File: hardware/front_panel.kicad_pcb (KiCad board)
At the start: 2 copper layers, 9.8 x 128.5 mm, 4 parts

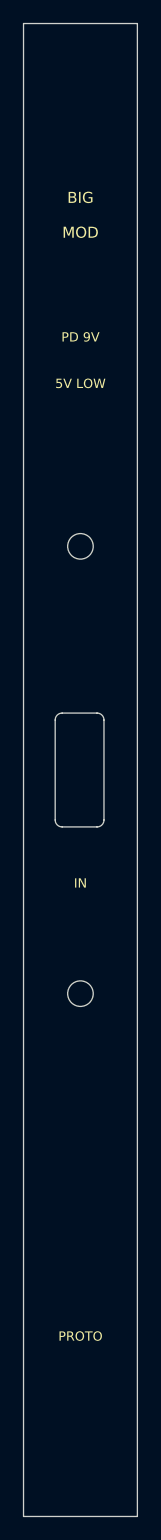
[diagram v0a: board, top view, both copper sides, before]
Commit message: WIP: consolidate PD-only Eurorack circuit on one sheet and dimension 2HP assembly
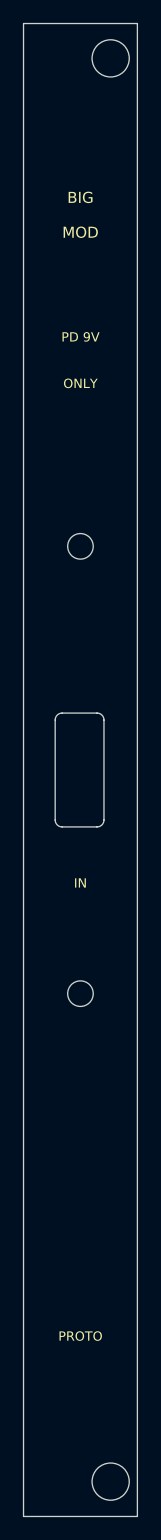
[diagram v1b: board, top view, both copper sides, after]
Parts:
- moved H1 2.60 mm to (57.5, 33.0)
- moved H2 2.60 mm to (57.5, 155.5)
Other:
- board text added: "Doepfer X=7.5 / dia3.2: 0.7mm FR4 web; M3 head overhang BLOCKER"
- board text added: "Mounting proposal: ../docs/assembly.svg / mechanics.md"
- board text added: "ONLY"
- board text removed: "5V LOW"
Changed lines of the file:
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@@
 	(footprint ""
 		(layer "F.Cu")
-		(at 54.9 113.5)
-		(property "Reference" "H4"
+		(at 57.5 155.5)
+		(property "Reference" "H2"
+			(at 0 0 0)
+			(layer "F.SilkS")
+			(hide yes)
+			(effects
+				(font
+					(size 1.27 1.27)
+				)
+			)
+		)
+		(property "Value" "MECHANICAL_NPTH"
+			(at 0 0 0)
+			(layer "F.Fab")
+			(hide yes)
+			(effects
+				(font
+					(size 1.27 1.27)
+				)
+			)
+		)
+		(property "Datasheet" ""
+			(at 0 0 0)
+			(layer "F.Fab")
+			(hide yes)
+			(effects
+				(font
+					(size 1.27 1.27)
+				)
+			)
+		)
+		(property "Description" ""
+			(at 0 0 0)
+			(layer "F.Fab")
+			(hide yes)
+			(effects
+				(font
+					(size 1.27 1.27)
+				)
+			)
+		)
+		(duplicate_pad_numbers_are_jumpers no)
+		(pad "" np_thru_hole circle
+			(at 0 0)
+			(size 3.2 3.2)
+			(drill 3.2)
+			(layers "*.Cu")
+		)
+		(embedded_fonts no)
+	)
+	(footprint ""
+		(layer "F.Cu")
+		(at 57.5 33)
+		(property "Reference" "H1"
+			(at 0 0 0)
+			(layer "F.SilkS")
+			(hide yes)
+			(effects
+				(font
+					(size 1.27 1.27)
+				)
+			)
+		)
+		(property "Value" "MECHANICAL_NPTH"
+			(at 0 0 0)
+			(layer "F.Fab")
+			(hide yes)
+			(effects
+				(font
+					(size 1.27 1.27)
+				)
+			)
+		)
+		(property "Datasheet" ""
+			(at 0 0 0)
+			(layer "F.Fab")
+			(hide yes)
+			(effects
+				(font
+					(size 1.27 1.27)
+				)
+			)
+		)
+		(property "Description" ""
+			(at 0 0 0)
+			(layer "F.Fab")
+			(hide yes)
+			(effects
+				(font
+					(size 1.27 1.27)
+				)
+			)
+		)
+		(duplicate_pad_numbers_are_jumpers no)
+		(pad "" np_thru_hole circle
+			(at 0 0)
+			(size 3.2 3.2)
+			(drill 3.2)
+			(layers "*.Cu")
+		)
+		(embedded_fonts no)
+	)
+	(footprint ""
+		(layer "F.Cu")
+		(at 54.9 75)
+		(property "Reference" "H3"
 			(at 0 0 0)
 			(layer "F.SilkS")
@@
 	(footprint ""
 		(layer "F.Cu")
-		(at 54.9 75)
-		(property "Reference" "H3"
+		(at 54.9 113.5)
+		(property "Reference" "H4"
 			(at 0 0 0)
 			(layer "F.SilkS")
@@
 		(embedded_fonts no)
 	)
-	(footprint ""
-		(layer "F.Cu")
-		(at 54.9 33)
-		(property "Reference" "H1"
-			(at 0 0 0)
-			(layer "F.SilkS")
-			(hide yes)
-			(effects
-				(font
-					(size 1.27 1.27)
-				)
-			)
-		)
-		(property "Value" "MECHANICAL_NPTH"
-			(at 0 0 0)
-			(layer "F.Fab")
-			(hide yes)
-			(effects
-				(font
-					(size 1.27 1.27)
-				)
-			)
-		)
-		(property "Datasheet" ""
-			(at 0 0 0)
-			(layer "F.Fab")
-			(hide yes)
-			(effects
-				(font
-					(size 1.27 1.27)
-				)
-			)
-		)
-		(property "Description" ""
-			(at 0 0 0)
-			(layer "F.Fab")
-			(hide yes)
-			(effects
-				(font
-					(size 1.27 1.27)
-				)
-			)
-		)
-		(duplicate_pad_numbers_are_jumpers no)
-		(pad "" np_thru_hole oval
-			(at 0 0)
-			(size 5 3.2)
-			(drill oval 5 3.2)
-			(layers "*.Cu")
-			(thermal_bridge_angle 45)
-		)
-		(embedded_fonts no)
-	)
-	(footprint ""
-		(layer "F.Cu")
-		(at 54.9 155.5)
-		(property "Reference" "H2"
-			(at 0 0 0)
-			(layer "F.SilkS")
-			(hide yes)
-			(effects
-				(font
-					(size 1.27 1.27)
-				)
-			)
-		)
-		(property "Value" "MECHANICAL_NPTH"
-			(at 0 0 0)
-			(layer "F.Fab")
-			(hide yes)
-			(effects
-				(font
-					(size 1.27 1.27)
-				)
-			)
-		)
-		(property "Datasheet" ""
-			(at 0 0 0)
-			(layer "F.Fab")
-			(hide yes)
-			(effects
-				(font
-					(size 1.27 1.27)
-				)
-			)
-		)
-		(property "Description" ""
-			(at 0 0 0)
-			(layer "F.Fab")
-			(hide yes)
-			(effects
-				(font
-					(size 1.27 1.27)
-				)
-			)
-		)
-		(duplicate_pad_numbers_are_jumpers no)
-		(pad "" np_thru_hole oval
-			(at 0 0)
-			(size 5 3.2)
-			(drill oval 5 3.2)
-			(layers "*.Cu")
-			(thermal_bridge_angle 45)
-		)
-		(embedded_fonts no)
-	)
 	(gr_line
 		(start 50 30)
@@
 		)
 	)
-	(gr_text "5V LOW"
+	(gr_text "ONLY"
 		(at 54.9 61 0)
 		(layer "F.SilkS")
@@
 				(thickness 0.12)
 			)
+		)
+	)
+	(gr_text "Mounting proposal: ../docs/assembly.svg / mechanics.md"
+		(at 112 70 0)
+		(layer "Dwgs.User")
+		(effects
+			(font
+				(size 0.85 0.85)
+				(thickness 0.12)
+			)
+		)
+	)
+	(gr_text "Doepfer X=7.5 / dia3.2: 0.7mm FR4 web; M3 head overhang BLOCKER"
+		(at 114 65 0)
+		(layer "Dwgs.User")
+		(effects
+			(font
+				(size 0.85 0.85)
+				(thickness 0.12)
+			)

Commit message: Update on the PCB.
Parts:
- added H5: MECHANICAL_NPTH, , F.Cu at (56.7, 68.0)
- added H6: MECHANICAL_NPTH, , F.Cu at (56.4, 121.0)
- moved H3 23.0 mm to (56.4, 52.0)
- moved H4 23.0 mm to (56.4, 136.5)
- moved H1 5.08 mm to (52.4, 33.0)
- moved H2 5.08 mm to (52.4, 155.5)
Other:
- outline, holes or cut-outs redrawn
- board text added: "2HP / round corner holes X2.42 = X7.50 minus one 5.08mm rail pitch"
- board text added: "A4.2"
- board text added: "A4.2 plain L brackets: M3x8 panel / M3x8 countersunk side"
- board text added: "PWR"
- board text added: "RESET"
- board text added: "TL3340AF160QG SMT recessed reset; 3mm THT LED formed 90 degrees"
- board text added: "USB"
- board text removed: "2HP: 9.8 x 128.5 x 1.6 mm"
- board text removed: "Doepfer X=7.5 / dia3.2: 0.7mm FR4 web; M3 head overhang BLOCKER"
- board text removed: "Front face Z=0; inward +Z; NO copper"
- board text removed: "IN"
- board text removed: "Mounting proposal: ../docs/assembly.svg / mechanics.md"
- board text removed: "ONLY"
- board text removed: "PROTO"
- board text removed: "Port axis (X,Y,Z)=(4.900,64.250,0.800)"
- board text removed: "USB cutout: 4.2 x 9.8, R0.6"

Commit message: Save 9 V power-supply schematic prototype and LED mechanical provisions
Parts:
- added H7: MECHANICAL_NPTH, , F.Cu at (56.7, 76.0)
- added H8: MECHANICAL_NPTH, , F.Cu at (56.7, 84.0)
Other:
- board text added: "+12V"
- board text added: "+5V"
- board text added: "-12V"
- board text added: "TL3340AF160QG SMT reset; D10/D11/D12 RED 3mm LEDs formed 90 degrees"
- board text removed: "PWR"
- board text removed: "TL3340AF160QG SMT recessed reset; 3mm THT LED formed 90 degrees"
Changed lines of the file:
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@@
+	(footprint ""
+		(layer "F.Cu")
+		(at 56.7 84)
+		(property "Reference" "H8"
+			(at 0 0 0)
+			(layer "F.SilkS")
+			(hide yes)
+			(effects
+				(font
+					(size 1.27 1.27)
+				)
+			)
+		)
+		(property "Value" "MECHANICAL_NPTH"
+			(at 0 0 0)
+			(layer "F.Fab")
+			(hide yes)
+			(effects
+				(font
+					(size 1.27 1.27)
+				)
+			)
+		)
+		(property "Datasheet" ""
+			(at 0 0 0)
+			(layer "F.Fab")
+			(hide yes)
+			(effects
+				(font
+					(size 1.27 1.27)
+				)
+			)
+		)
+		(property "Description" ""
+			(at 0 0 0)
+			(layer "F.Fab")
+			(hide yes)
+			(effects
+				(font
+					(size 1.27 1.27)
+				)
+			)
+		)
+		(duplicate_pad_numbers_are_jumpers no)
+		(pad "" np_thru_hole circle
+			(at 0 0)
+			(size 3.6 3.6)
+			(drill 3.6)
+			(layers "*.Cu")
+		)
+		(embedded_fonts no)
+	)
 	(footprint ""
 		(layer "F.Cu")
@@
 		(at 56.7 68)
 		(property "Reference" "H5"
+			(at 0 0 0)
+			(layer "F.SilkS")
+			(hide yes)
+			(effects
+				(font
+					(size 1.27 1.27)
+				)
+			)
+		)
+		(property "Value" "MECHANICAL_NPTH"
+			(at 0 0 0)
+			(layer "F.Fab")
+			(hide yes)
+			(effects
+				(font
+					(size 1.27 1.27)
+				)
+			)
+		)
+		(property "Datasheet" ""
+			(at 0 0 0)
+			(layer "F.Fab")
+			(hide yes)
+			(effects
+				(font
+					(size 1.27 1.27)
+				)
+			)
+		)
+		(property "Description" ""
+			(at 0 0 0)
+			(layer "F.Fab")
+			(hide yes)
+			(effects
+				(font
+					(size 1.27 1.27)
+				)
+			)
+		)
+		(duplicate_pad_numbers_are_jumpers no)
+		(pad "" np_thru_hole circle
+			(at 0 0)
+			(size 3.6 3.6)
+			(drill 3.6)
+			(layers "*.Cu")
+		)
+		(embedded_fonts no)
+	)
+	(footprint ""
+		(layer "F.Cu")
+		(at 56.7 76)
+		(property "Reference" "H7"
 			(at 0 0 0)
 			(layer "F.SilkS")
@@
 		(layer "Edge.Cuts")
 	)
-	(gr_text "PWR"
-		(at 54.9 63 0)
+	(gr_text "+12V"
+		(at 54.9 64 0)
 		(layer "F.SilkS")
 		(effects
@@
 		)
 	)
-	(gr_text "PD 9V"
-		(at 54.9 84 0)
+	(gr_text "-12V"
+		(at 54.9 72 0)
+		(layer "F.SilkS")
+		(effects
+			(font
+				(size 0.8 0.8)
+				(thickness 0.12)
+			)
+		)
+	)
+	(gr_text "+5V"
+		(at 54.9 80 0)
 		(layer "F.SilkS")
 		(effects
@@
 		)
 	)
+	(gr_text "PD 9V"
+		(at 54.9 106.5 0)
+		(layer "F.SilkS")
+		(effects
+			(font
+				(size 0.8 0.8)
+				(thickness 0.12)
+			)
+		)
+	)
 	(gr_text "RESET"
 		(at 54.9 116 0)
@@
 		)
 	)
-	(gr_text "TL3340AF160QG SMT recessed reset; 3mm THT LED formed 90 degrees"
+	(gr_text "TL3340AF160QG SMT reset; D10/D11/D12 RED 3mm LEDs formed 90 degrees"
 		(at 100 48 0)
 		(layer "Dwgs.User")

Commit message: Replace MCU diagnostics with optional rail-sense IDC and single 5 V power LED
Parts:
- removed H7, H8: MECHANICAL_NPTH, 
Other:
- board text added: "+5V POWER"
- board text added: "TL3340AF160QG SMT reset; D10 RED 3mm +5V power LED formed 90 degrees"
- board text removed: "+12V"
- board text removed: "+5V"
- board text removed: "-12V"
- board text removed: "TL3340AF160QG SMT reset; D10/D11/D12 RED 3mm LEDs formed 90 degrees"

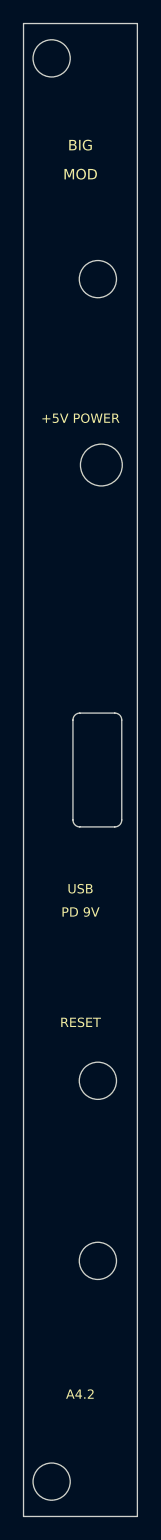
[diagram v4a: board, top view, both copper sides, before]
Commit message: Move USB, retry button and power LED to top; synchronize 64 V1 footprints without routing
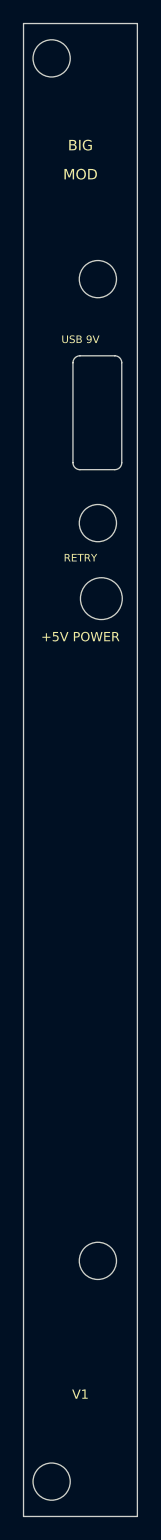
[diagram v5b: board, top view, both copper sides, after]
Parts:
- moved ? 48.0 mm to (56.4, 73.0)
- moved ? 11.5 mm to (56.7, 79.5)
- renumbered H3 to ?, H4 to ?, H1 to ?, H6 to ?, H2 to ?, H5 to ?
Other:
- outline, holes or cut-outs redrawn
- board text added: "RETRY"
- board text added: "USB 9V"
- board text added: "V1"
- board text removed: "A4.2"
- board text removed: "PD 9V"
- board text removed: "RESET"
- board text removed: "USB"

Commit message: Swap retry switch and power LED positions on carrier and front panel
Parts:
- moved ? 6.50 mm to (56.4, 79.5)
- moved ? 6.50 mm to (56.7, 73.0)
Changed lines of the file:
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@@
 	(footprint ""
 		(layer "F.Cu")
-		(at 56.4 73)
+		(at 56.4 79.5)
 		(property "Reference" ""
 			(at 0 0 0)
@@
 	(footprint ""
 		(layer "F.Cu")
-		(at 56.7 79.5)
+		(at 56.7 73)
 		(property "Reference" ""
 			(at 0 0 0)
@@
 	)
 	(gr_text "RETRY"
-		(at 54.9 76 0)
+		(at 54.9 82.5 0)
 		(layer "F.SilkS")
 		(effects
@@
 	)
 	(gr_text "+5V POWER"
-		(at 54.9 82.8 0)
+		(at 54.9 76.3 0)
 		(layer "F.SilkS")
 		(effects

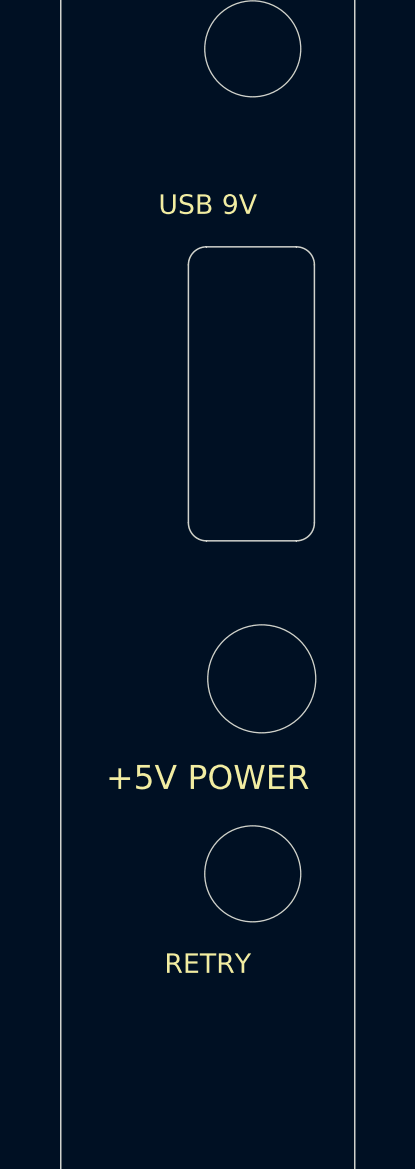
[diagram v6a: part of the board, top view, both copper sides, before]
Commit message: Complete four-layer routing, adopt proven HRO USB-C and release checked fabrication files
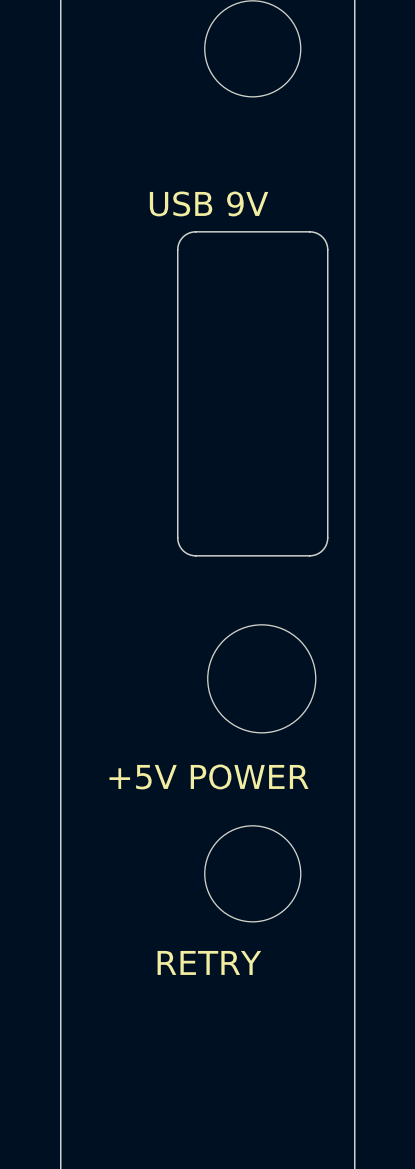
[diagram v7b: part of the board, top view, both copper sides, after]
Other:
- outline, holes or cut-outs redrawn
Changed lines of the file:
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@@
 	)
 	(setup
+		(stackup
+ (layer "F.SilkS" (type "Top Silk Screen") (color "White"))
+ (layer "F.Paste" (type "Top Solder Paste"))
+ (layer "F.Mask" (type "Top Solder Mask") (color "Black") (thickness 0.01))
+ (layer "F.Cu" (type "copper") (thickness 0))
+ (layer "dielectric 1" (type "core") (thickness 1.58) (material "FR4 Tg170") (epsilon_r 4.5) (loss_tangent 0.02))
+ (layer "B.Cu" (type "copper") (thickness 0))
+ (layer "B.Mask" (type "Bottom Solder Mask") (color "Black") (thickness 0.01))
+ (layer "B.Paste" (type "Bottom Solder Paste"))
+ (layer "B.SilkS" (type "Bottom Silk Screen") (color "White"))
+ (copper_finish "None") (dielectric_constraints no))
 		(pad_to_mask_clearance 0)
 		(allow_soldermask_bridges_in_footprints no)
@@
 		(attr board_only exclude_from_pos_files exclude_from_bom)
 		(duplicate_pad_numbers_are_jumpers no)
+		(fp_circle
+			(center 0 0)
+			(end 3.75 0)
+			(stroke
+				(width 0.05)
+				(type default)
+			)
+			(fill no)
+			(layer "F.CrtYd")
+		)
 		(pad "" np_thru_hole circle
 			(at 0 0)
@@
 		(attr board_only exclude_from_pos_files exclude_from_bom)
 		(duplicate_pad_numbers_are_jumpers no)
+		(fp_circle
+			(center 0 0)
+			(end 3.75 0)
+			(stroke
+				(width 0.05)
+				(type default)
+			)
+			(fill no)
+			(layer "F.CrtYd")
+		)
 		(pad "" np_thru_hole circle
 			(at 0 0)
@@
 		(attr board_only exclude_from_pos_files exclude_from_bom)
 		(duplicate_pad_numbers_are_jumpers no)
+		(fp_circle
+			(center 0 0)
+			(end 3.25 0)
+			(stroke
+				(width 0.05)
+				(type default)
+			)
+			(fill no)
+			(layer "F.CrtYd")
+		)
 		(pad "" np_thru_hole circle
 			(at 0 0)
@@
 		(attr board_only exclude_from_pos_files exclude_from_bom)
 		(duplicate_pad_numbers_are_jumpers no)
+		(fp_circle
+			(center 0 0)
+			(end 1.85 0)
+			(stroke
+				(width 0.05)
+				(type default)
+			)
+			(fill no)
+			(layer "F.CrtYd")
+		)
 		(pad "" np_thru_hole circle
 			(at 0 0)
@@
 		(attr board_only exclude_from_pos_files exclude_from_bom)
 		(duplicate_pad_numbers_are_jumpers no)
+		(fp_circle
+			(center 0 0)
+			(end 3.25 0)
+			(stroke
+				(width 0.05)
+				(type default)
+			)
+			(fill no)
+			(layer "F.CrtYd")
+		)
 		(pad "" np_thru_hole circle
 			(at 0 0)
@@
 		(attr board_only exclude_from_pos_files exclude_from_bom)
 		(duplicate_pad_numbers_are_jumpers no)
+		(fp_circle
+			(center 0 0)
+			(end 2.05 0)
+			(stroke
+				(width 0.05)
+				(type default)
+			)
+			(fill no)
+			(layer "F.CrtYd")
+		)
 		(pad "" np_thru_hole circle
 			(at 0 0)
@@
 	)
 	(gr_arc
-		(start 54.255 59.2)
-		(mid 54.430735 58.775735)
-		(end 54.855 58.6)
+		(start 53.9 58.7)
+		(mid 54.075735 58.275735)
+		(end 54.5 58.1)
 		(stroke
 			(width 0.05)
@@
 	)
 	(gr_line
-		(start 54.255 67.8)
-		(end 54.255 59.2)
+		(start 53.9 68.3)
+		(end 53.9 58.7)
 		(stroke
 			(width 0.05)
@@
 	)
 	(gr_line
-		(start 54.855 58.6)
-		(end 57.855 58.6)
+		(start 54.5 58.1)
+		(end 58.3 58.1)
 		(stroke
 			(width 0.05)
@@
 	)
 	(gr_arc
-		(start 54.855 68.4)
-		(mid 54.430735 68.224264)
-		(end 54.255 67.8)
+		(start 54.5 68.9)
+		(mid 54.075735 68.724264)
+		(end 53.9 68.3)
 		(stroke
 			(width 0.05)
@@
 	)
 	(gr_arc
-		(start 57.855 58.6)
-		(mid 58.279264 58.775735)
-		(end 58.455 59.2)
+		(start 58.3 58.1)
+		(mid 58.724264 58.275735)
+		(end 58.9 58.7)
 		(stroke
 			(width 0.05)
@@
 	)
 	(gr_line
-		(start 57.855 68.4)
-		(end 54.855 68.4)
+		(start 58.3 68.9)
+		(end 54.5 68.9)
 		(stroke
 			(width 0.05)
@@
 	)
 	(gr_line
-		(start 58.455 59.2)
-		(end 58.455 67.8)
+		(start 58.9 58.7)
+		(end 58.9 68.3)
 		(stroke
 			(width 0.05)
@@
 	)
 	(gr_arc
-		(start 58.455 67.8)
-		(mid 58.279264 68.224264)
-		(end 57.855 68.4)
+		(start 58.9 68.3)
+		(mid 58.724264 68.724264)
+		(end 58.3 68.9)
 		(stroke
 			(width 0.05)
@@
 		(effects
 			(font
-				(size 0.65 0.65)
+				(size 0.8 0.8)
+				(thickness 0.12)
+			)
+		)
+	)
+	(gr_text "+5V POWER"
+		(at 54.9 76.3 0)
+		(layer "F.SilkS")
+		(effects
+			(font
+				(size 0.8 0.8)
 				(thickness 0.12)
 			)
@@
 		(layer "F.SilkS")
 		(effects
-			(font
-				(size 0.65 0.65)
-				(thickness 0.12)
-			)
-		)
-	)
-	(gr_text "+5V POWER"
-		(at 54.9 76.3 0)
-		(layer "F.SilkS")
-		(effects
